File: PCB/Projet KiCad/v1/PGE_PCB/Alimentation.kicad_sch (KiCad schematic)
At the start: 18 parts, among them CN1 Conn_01x02, J3 Conn_01x03, U5 MCP73831T, U6 DS2438AZ+

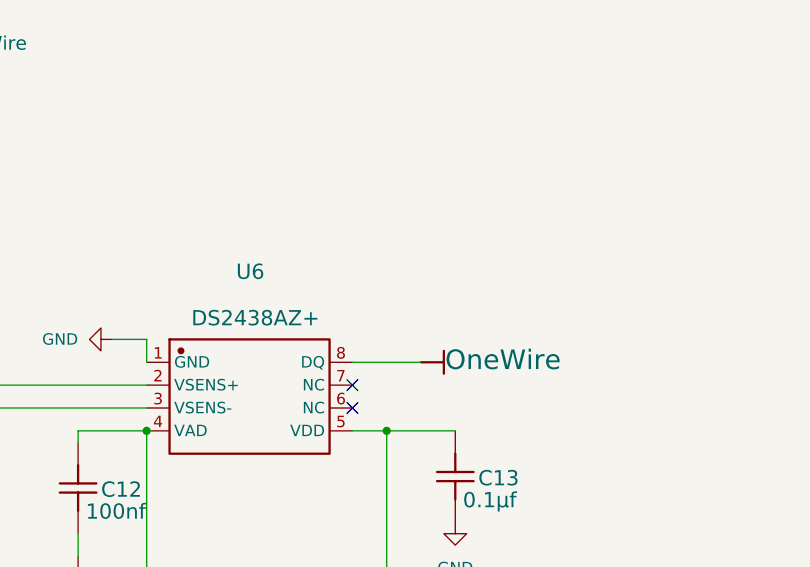
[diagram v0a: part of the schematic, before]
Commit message: Ajout d'une resistance de pullup sur la ligne OneWire
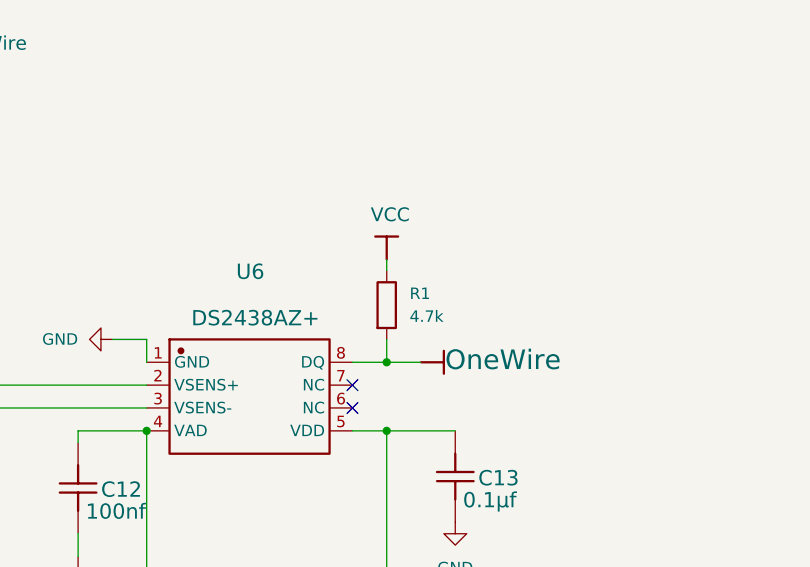
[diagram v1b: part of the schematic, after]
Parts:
- added R1: 4.7k, Resistor_SMD:R_0805_2012Metric, symbol Device:R
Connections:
- net OneWire: now also R1.2
- net VCC: now also R1.1
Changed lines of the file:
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@@
 	)
 	(junction
+		(at 215.9 72.39)
+		(diameter 0)
+		(color 0 0 0 0)
+	)
+	(junction
 		(at 62.23 85.09)
 		(diameter 0)
@@
 	(wire
 		(pts
-			(xy 219.71 72.39) (xy 212.09 72.39)
+			(xy 219.71 72.39) (xy 215.9 72.39)
 		)
 		(stroke
@@
 	(wire
 		(pts
+			(xy 215.9 60.96) (xy 215.9 62.23)
+		)
+		(stroke
+			(width 0)
+			(type default)
+		)
+	)
+	(wire
+		(pts
 			(xy 88.9 99.06) (xy 88.9 100.33)
 		)
@@
 	(wire
 		(pts
+			(xy 215.9 72.39) (xy 212.09 72.39)
+		)
+		(stroke
+			(width 0)
+			(type default)
+		)
+	)
+	(wire
+		(pts
 			(xy 152.4 77.47) (xy 165.1 77.47)
 		)
@@
 	(wire
 		(pts
+			(xy 215.9 69.85) (xy 215.9 72.39)
+		)
+		(stroke
+			(width 0)
+			(type default)
+		)
+	)
+	(wire
+		(pts
 			(xy 110.49 34.29) (xy 110.49 36.83)
 		)
@@
 	)
 	(symbol
+		(lib_id "VCC")
+		(at 215.9 60.96 0)
+		(mirror x)
+		(unit 0)
+		(exclude_from_sim no)
+		(in_bom yes)
+		(on_board yes)
+		(dnp no)
+		(property "Reference" "#PWR01"
+			(at 215.9 60.96 0)
+			(effects
+				(font
+					(size 1.27 1.27)
+				)
+				(hide yes)
+			)
+		)
+		(property "Value" "VCC"
+			(at 214.122 56.896 0)
+			(effects
+				(font
+					(size 1.524 1.524)
+				)
+				(justify left top)
+			)
+		)
+		(property "Footprint" ""
+			(at 215.9 60.96 0)
+			(effects
+				(font
+					(size 1.27 1.27)
+				)
+				(hide yes)
+			)
+		)
+		(property "Datasheet" ""
+			(at 215.9 60.96 0)
+			(effects
+				(font
+					(size 1.27 1.27)
+				)
+				(hide yes)
+			)
+		)
+		(property "Description" "Le symbole d'alimentation crée un label global de nom 'VCC'"
+			(at 215.9 60.96 0)
+			(effects
+				(font
+					(size 1.27 1.27)
+				)
+				(hide yes)
+			)
+		)
+		(pin "1"
+		)
+		(instances
+			(project "Alimentation"
+				(path "/7e6bc5b4-5d5a-4fe9-b3ba-e1e3489293c3"
+					(reference "#PWR01")
+					(unit 0)
+				)
+			)
+		)
+	)
+	(symbol
 		(lib_id "power:GND")
 		(at 88.9 100.33 0)
@@
 				)
 			)
+			(project "Alimentation"
+				(path "/7e6bc5b4-5d5a-4fe9-b3ba-e1e3489293c3"
+					(reference "R11")
+					(unit 1)
+				)
+			)
 		)
 	)
@@
 	)
 	(symbol
+		(lib_id "Device:R")
+		(at 215.9 66.04 0)
+		(unit 1)
+		(exclude_from_sim no)
+		(in_bom yes)
+		(on_board yes)
+		(dnp no)
+		(fields_autoplaced yes)
+		(property "Reference" "R1"
+			(at 218.44 64.7699 0)
+			(effects
+				(font
+					(size 1.27 1.27)
+				)
+				(justify left)
+			)
+		)
+		(property "Value" "4.7k"
+			(at 218.44 67.3099 0)
+			(effects
+				(font
+					(size 1.27 1.27)
+				)
+				(justify left)
+			)
+		)
+		(property "Footprint" "Resistor_SMD:R_0805_2012Metric"
+			(at 214.122 66.04 90)
+			(effects
+				(font
+					(size 1.27 1.27)
+				)
+				(hide yes)
+			)
+		)
+		(property "Datasheet" "~"
+			(at 215.9 66.04 0)
+			(effects
+				(font
+					(size 1.27 1.27)
+				)
+				(hide yes)
+			)
+		)
+		(property "Description" "Resistor"
+			(at 215.9 66.04 0)
+			(effects
+				(font
+					(size 1.27 1.27)
+				)
+				(hide yes)
+			)
+		)
+		(pin "2"
+		)
+		(pin "1"
+		)
+		(instances
+			(project "Alimentation"
+				(path "/7e6bc5b4-5d5a-4fe9-b3ba-e1e3489293c3"
+					(reference "R1")
+					(unit 1)
+				)
+			)
+		)
+	)
+	(symbol
 		(lib_id "Vbat+")
 		(at 110.49 36.83 0)
@@
 		)
 	)
+	(sheet_instances
+		(path "/"
+			(page "1")
+		)
+	)

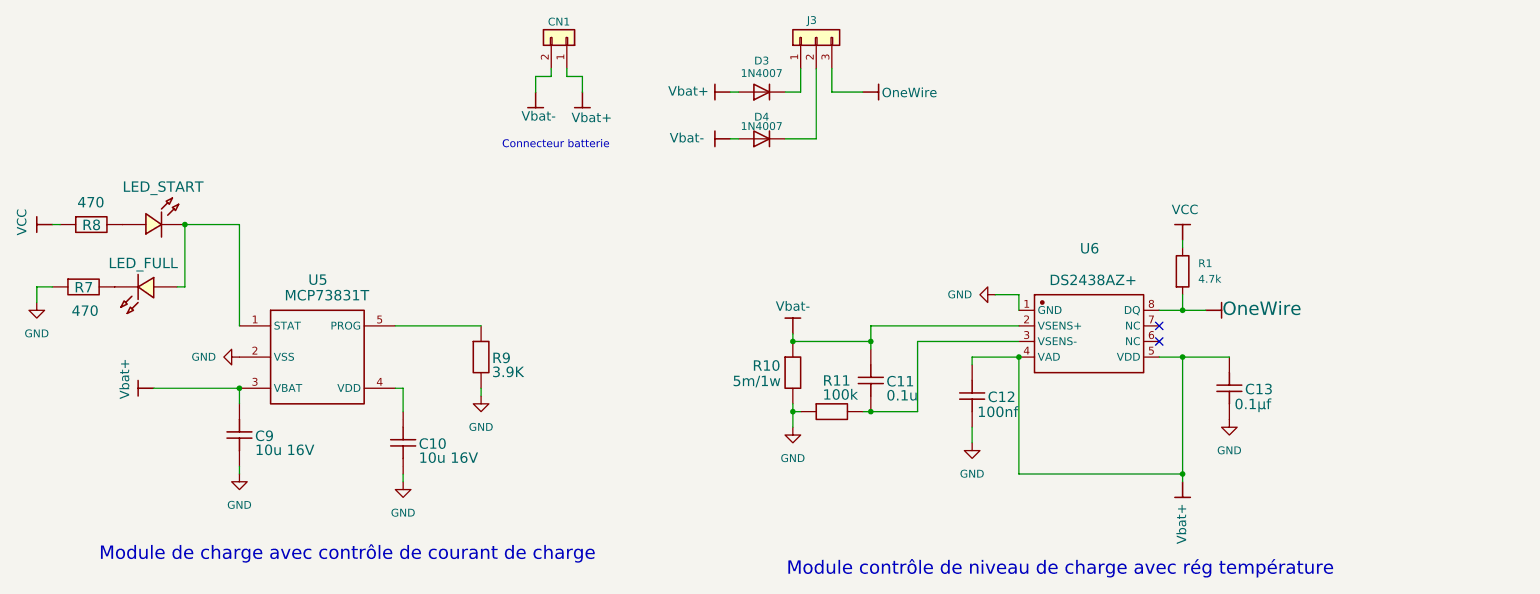
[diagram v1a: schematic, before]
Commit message: Maj PCB
- correction module GPS (I2C)
- ajout module LoRa RFM9x
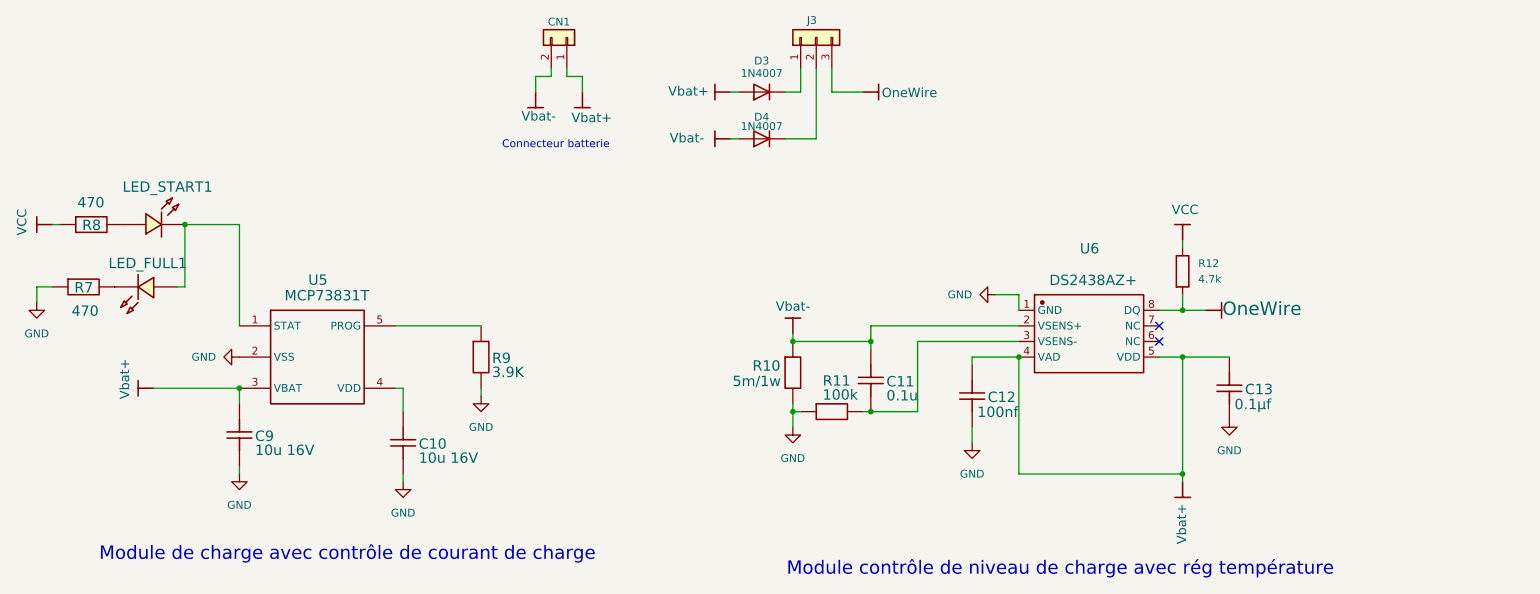
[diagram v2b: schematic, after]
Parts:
- renumbered LED_FULL to LED_FULL1, LED_START to LED_START1, R1 to R12
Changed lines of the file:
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@@
 		(at 215.9 60.96 0)
 		(mirror x)
-		(unit 0)
-		(exclude_from_sim no)
-		(in_bom yes)
-		(on_board yes)
-		(dnp no)
-		(property "Reference" "#PWR01"
+		(unit 1)
+		(exclude_from_sim no)
+		(in_bom yes)
+		(on_board yes)
+		(dnp no)
+		(property "Reference" "#PWR0101"
 			(at 215.9 60.96 0)
 			(effects
@@
 		)
 		(instances
+			(project "PGE_PCB"
+				(path "/503a3176-3dc5-409a-9acd-b4c6a6fcf256/7b7c49ad-28b8-4456-8a93-99baeb169400"
+					(reference "#PWR0101")
+					(unit 1)
+				)
+			)
 			(project "Alimentation"
 				(path "/7e6bc5b4-5d5a-4fe9-b3ba-e1e3489293c3"
@@
 		(dnp no)
 		(fields_autoplaced yes)
-		(property "Reference" "R1"
+		(property "Reference" "R12"
 			(at 218.44 64.7699 0)
 			(effects
@@
 		)
 		(instances
+			(project "PGE_PCB"
+				(path "/503a3176-3dc5-409a-9acd-b4c6a6fcf256/7b7c49ad-28b8-4456-8a93-99baeb169400"
+					(reference "R12")
+					(unit 1)
+				)
+			)
 			(project "Alimentation"
 				(path "/7e6bc5b4-5d5a-4fe9-b3ba-e1e3489293c3"
@@
 		(on_board yes)
 		(dnp no)
-		(property "Reference" "LED_START"
+		(property "Reference" "LED_START1"
 			(at 43.18 51.308 0)
 			(effects
@@
 			(project "PGE_PCB"
 				(path "/503a3176-3dc5-409a-9acd-b4c6a6fcf256/7b7c49ad-28b8-4456-8a93-99baeb169400"
-					(reference "LED_START")
+					(reference "LED_START1")
 					(unit 1)
 				)
@@
 		(on_board yes)
 		(dnp no)
-		(property "Reference" "LED_FULL"
+		(property "Reference" "LED_FULL1"
 			(at 40.894 63.754 0)
 			(effects
@@
 			(project "PGE_PCB"
 				(path "/503a3176-3dc5-409a-9acd-b4c6a6fcf256/7b7c49ad-28b8-4456-8a93-99baeb169400"
-					(reference "LED_FULL")
-					(unit 1)
-				)
+					(reference "LED_FULL1")
+					(unit 1)
+				)
